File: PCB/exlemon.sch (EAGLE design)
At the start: 11 parts

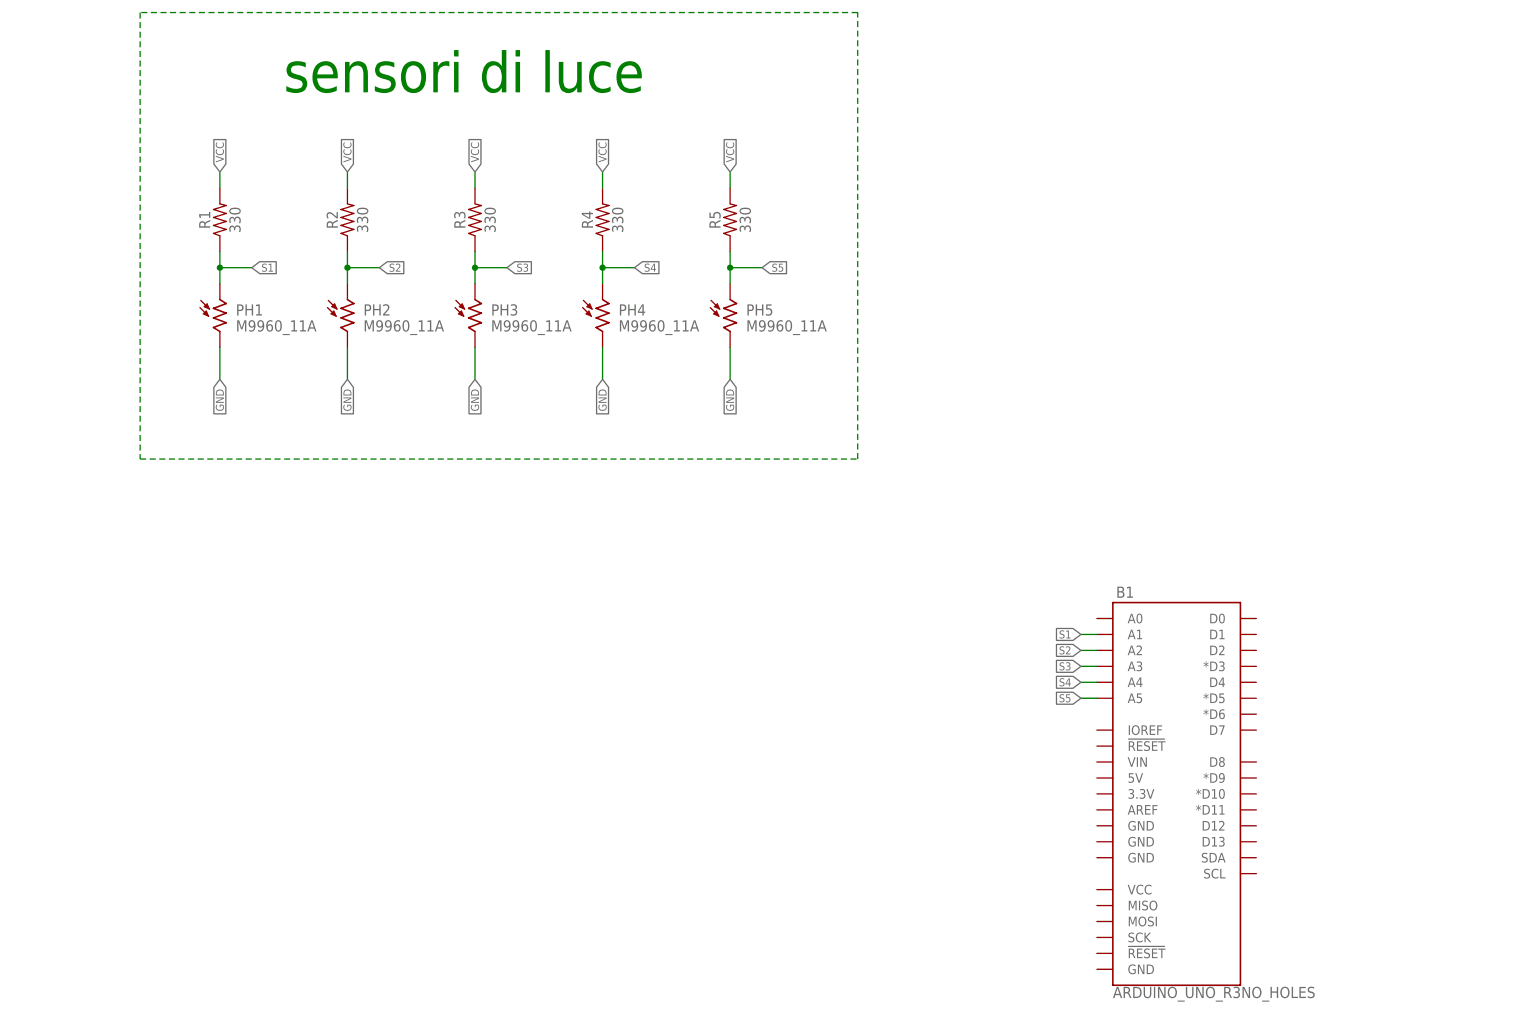
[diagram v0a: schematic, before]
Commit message: PCB con bumper e ultrasuoni
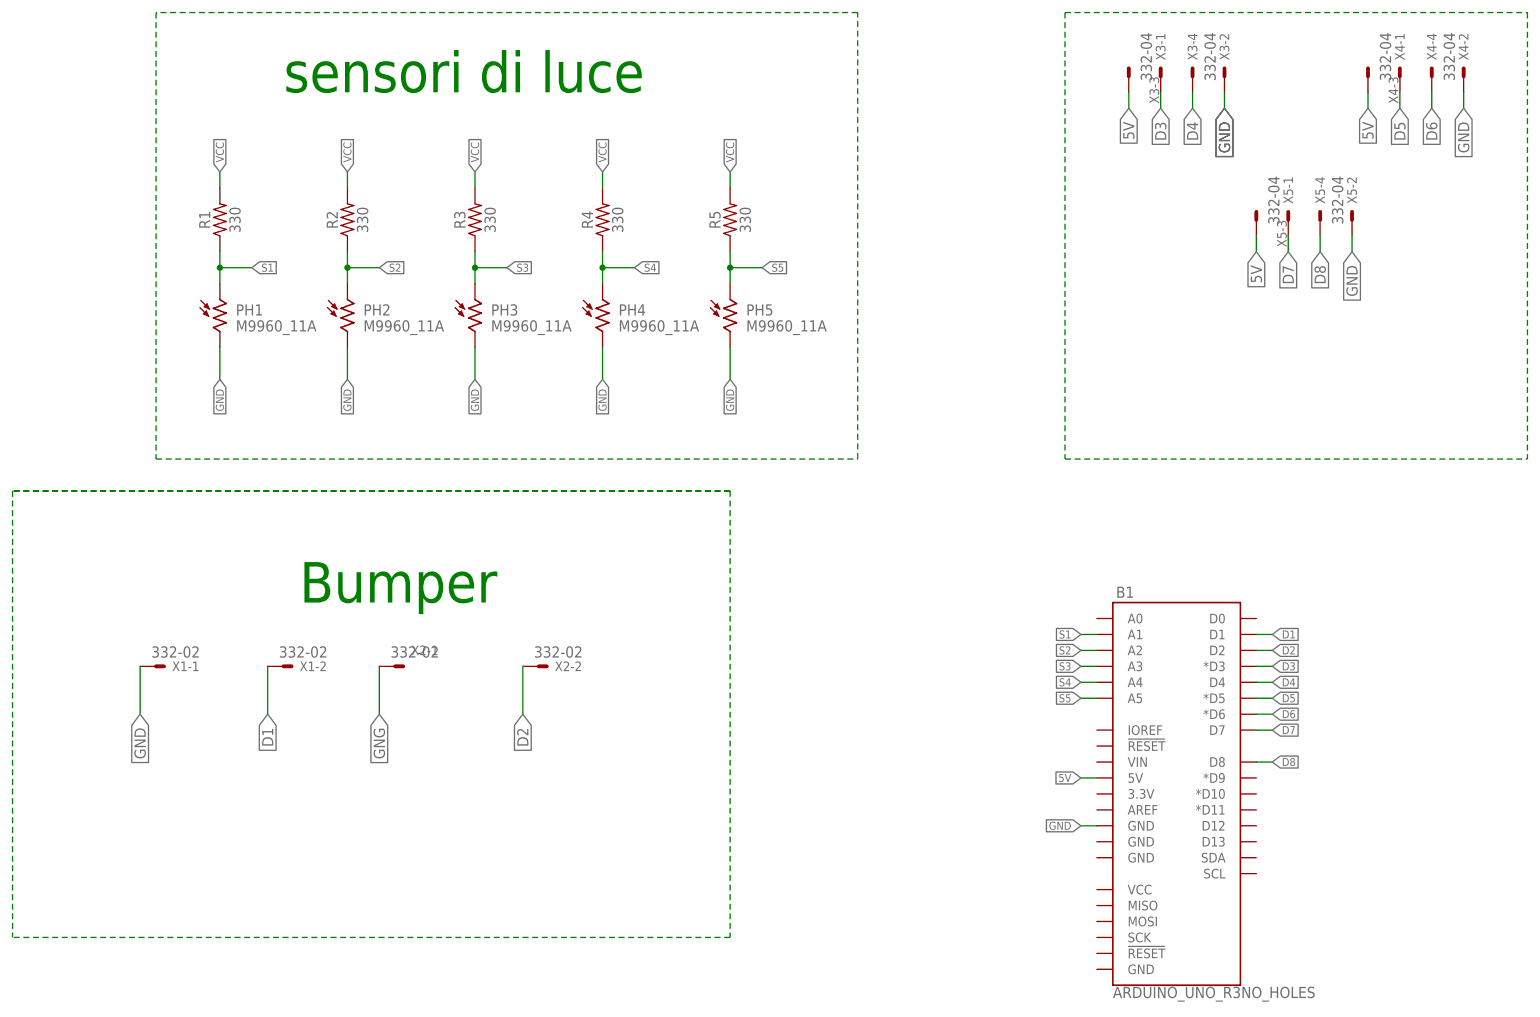
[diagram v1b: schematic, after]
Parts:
- added X1, X2: 332-02, con-garry:332-02
- added X3, X4, X5: 332-04, con-garry:332-04
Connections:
- new net 5V: B1.5V, X3-3.S, X4-3.S, X5-3.S
- new net D1: B1.D1, X1-2.S
- new net D2: B1.D2, X2-2.S
- new net D3: B1.*D3, X3-1.S
- new net D4: B1.D4, X3-4.S
- new net D5: B1.*D5, X4-1.S
- new net D6: B1.*D6, X4-4.S
- new net D7: B1.D7, X5-1.S
- new net D8: B1.D8, X5-4.S
- new net GNG: X2-1.S
- new net N$9: X4-2.S
- net GND: now also B1.GND@2, X1-1.S, X3-2.S, X5-2.S
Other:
- note added: "Bumper"
